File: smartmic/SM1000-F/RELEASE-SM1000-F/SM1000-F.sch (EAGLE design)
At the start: 214 parts, among them CN1 HDR100-3, CN10 ST-3509, CN11 HDR100-3, CN12 DIL16X300, CN2 JS-MU3-002, CN3 DS-0518, CN4 RJ-45, CN5 ST-3509, CN6 ST-3509, CN7 ST-3509, CN8 ST-3509, CN9 ST-3509, J1 JMP-2PIN, J2 JMP-2PIN, J3 JMP-2PIN, J4 CONN-BOOM-XH-2A, J5 JMP-2PIN, P1 TPAD50, P10 TPAD50, P11 TPAD50, P12 TPAD50, P13 TPAD50, P14 TPAD50, P15 TPAD50, P16 TPAD50, P17 TPAD50, P18 TPAD50, P19 TPAD50, P2 TPAD50, P20 TPAD50, P21 TPAD50, P3 TPAD50, P4 TPAD50, P5 TPAD50, P6 TPAD50, P7 TPAD50, P8 TPAD50, P9 TPAD50, SW1 SW-LC2259, SW2 TS-026, SW3 SW-LC2259EENP, SW4 TS-026, SW5 TS-02B, T1 SM-LP-5001, T2 SM-LP-5001, U1 STM32F405VGT6, U10 DNL, U2 LD3985M33R, U3 STMPS2141, U4 EMIF02-USB03F2, U5 TPS54329E, U6 LMV341, U7 LMV341, U8 LM386M-1, U9 LMV341

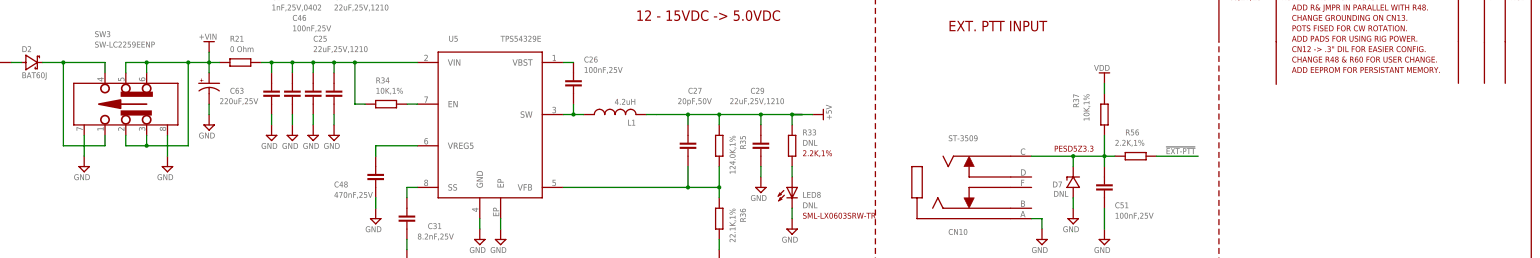
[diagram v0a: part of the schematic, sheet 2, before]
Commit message: removed GNDs from SW1 & SW3 mounting tabs
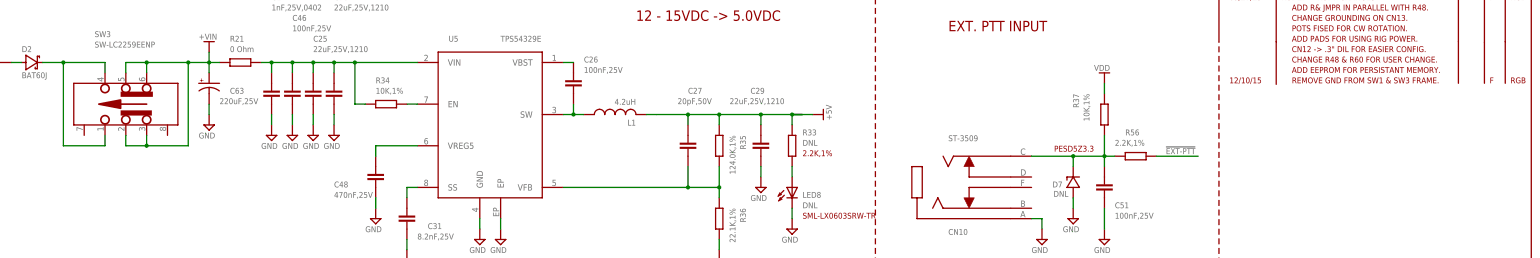
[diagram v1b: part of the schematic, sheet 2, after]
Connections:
- net GND: no longer SW1.7, SW1.8, SW3.7, SW3.8
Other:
- note added: "12/10/15"
- note added: "REMOVE GND FROM SW1 & SW3 FRAME."
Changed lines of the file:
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@@
 <part name="CN9" library="_RoweTel" deviceset="ST-3509" device=""/>
 <part name="CN10" library="_RoweTel" deviceset="ST-3509" device=""/>
-<part name="V49" library="A-SUPPLY2" deviceset="GND" device=""/>
 <part name="SW2" library="_RoweTel" deviceset="TS-026" device=""/>
 <part name="SW4" library="_RoweTel" deviceset="TS-026" device=""/>
@@
 <part name="J4" library="_RoweTel" deviceset="CONN-BOOM-XH-2A" device=""/>
 <part name="V120" library="A-SUPPLY2" deviceset="VDD" device=""/>
-<part name="V121" library="A-SUPPLY2" deviceset="GND" device=""/>
-<part name="V141" library="A-SUPPLY2" deviceset="GND" device=""/>
 <part name="J2" library="_Coherix" deviceset="JMP-2PIN" device=""/>
 <part name="SH2" library="_Coherix" deviceset="SHUNT,0.1IN" device=""/>
@@
 <text x="391.668" y="134.62" size="1.4224" layer="94" ratio="10" rot="R90">4.7K,1%</text>
 <text x="399.542" y="134.62" size="1.4224" layer="94" ratio="10" rot="R90">4.7K,1%</text>
+<text x="373.38" y="254" size="1.4224" layer="94" ratio="10">REMOVE GND FROM SW1 &amp; SW3 FRAME.</text>
+<text x="358.14" y="254" size="1.4224" layer="94" ratio="10">12/10/15</text>
+<text x="421.64" y="254" size="1.4224" layer="94" ratio="10">F</text>
+<text x="426.72" y="254" size="1.4224" layer="94" ratio="10">RGB</text>
 </plain>
 <instances>
@@
 <attribute name="VALUE" x="297.18" y="157.48" size="1.4224" layer="96" ratio="9"/>
 </instance>
-<instance part="V49" gate="GND" x="185.42" y="233.68"/>
 <instance part="SW2" gate="G$1" x="241.3" y="241.3" smashed="yes" rot="R270">
 <attribute name="NAME" x="254" y="243.84" size="1.4224" layer="95" ratio="10"/>
@@
 <wire x1="284.48" y1="231.14" x2="281.94" y2="231.14" width="0.1524" layer="91"/>
 <junction x="281.94" y="231.14"/>
-</segment>
-<segment>
-<wire x1="185.42" y1="264.16" x2="185.42" y2="243.84" width="0.1524" layer="91"/>
-<wire x1="185.42" y1="243.84" x2="185.42" y2="236.22" width="0.1524" layer="91"/>
-<pinref part="V49" gate="GND" pin="GND"/>
-<pinref part="SW1" gate="G$1" pin="8"/>
-<wire x1="185.42" y1="264.16" x2="190.5" y2="264.16" width="0.1524" layer="91"/>
-<pinref part="SW1" gate="G$1" pin="7"/>
-<wire x1="185.42" y1="243.84" x2="190.5" y2="243.84" width="0.1524" layer="91"/>
-<junction x="185.42" y="243.84"/>
 </segment>
 <segment>
@@
 <wire x1="422.91" y1="264.16" x2="422.91" y2="254" width="0.1524" layer="94"/>
 <text x="370.84" y="256.54" size="1.4224" layer="94" ratio="10">ADD EEPROM FOR PERSISTANT MEMORY.</text>
+<text x="370.84" y="254" size="1.4224" layer="94" ratio="10">REMOVE GND FROM SW1 &amp; SW3 FRAME.</text>
+<text x="355.6" y="254" size="1.4224" layer="94" ratio="10">12/10/15</text>
+<text x="419.1" y="254" size="1.4224" layer="94" ratio="10">F</text>
+<text x="424.18" y="254" size="1.4224" layer="94" ratio="10">RGB</text>
 </plain>
 <instances>
@@
 <attribute name="NAME" x="121.92" y="30.48" size="1.4224" layer="95" ratio="10"/>
 <attribute name="VALUE" x="114.3" y="27.94" size="1.4224" layer="95" ratio="10"/>
-</instance>
-<instance part="V121" gate="GND" x="96.52" y="233.68" smashed="yes">
-<attribute name="VALUE" x="93.98" y="230.378" size="1.4224" layer="96" ratio="9"/>
-</instance>
-<instance part="V141" gate="GND" x="76.2" y="233.68" smashed="yes">
-<attribute name="VALUE" x="73.66" y="230.378" size="1.4224" layer="96" ratio="9"/>
 </instance>
 <instance part="J2" gate="G$1" x="124.46" y="48.26" smashed="yes" rot="R90">
@@
 </segment>
 <segment>
-<pinref part="SW3" gate="G$1" pin="7"/>
-<pinref part="V141" gate="GND" pin="GND"/>
-<wire x1="76.2" y1="241.3" x2="76.2" y2="236.22" width="0.1524" layer="91"/>
-</segment>
-<segment>
-<pinref part="V121" gate="GND" pin="GND"/>
-<pinref part="SW3" gate="G$1" pin="8"/>
-<wire x1="96.52" y1="236.22" x2="96.52" y2="241.3" width="0.1524" layer="91"/>
-</segment>
-<segment>
